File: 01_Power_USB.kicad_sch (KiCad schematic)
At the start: 11 parts, among them J1 UJC-HP-3-SMT-TR, U3 TLV75533PDBVR, U5 TPD2E2U06DCK

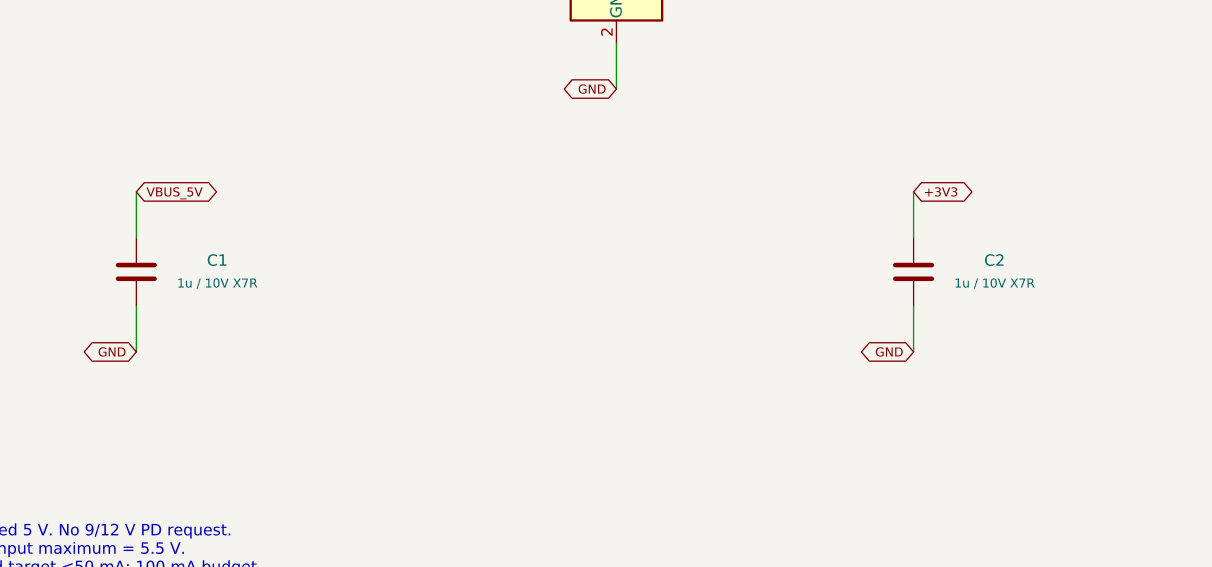
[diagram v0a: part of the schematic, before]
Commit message: Complete procurement BOM and document component review gates
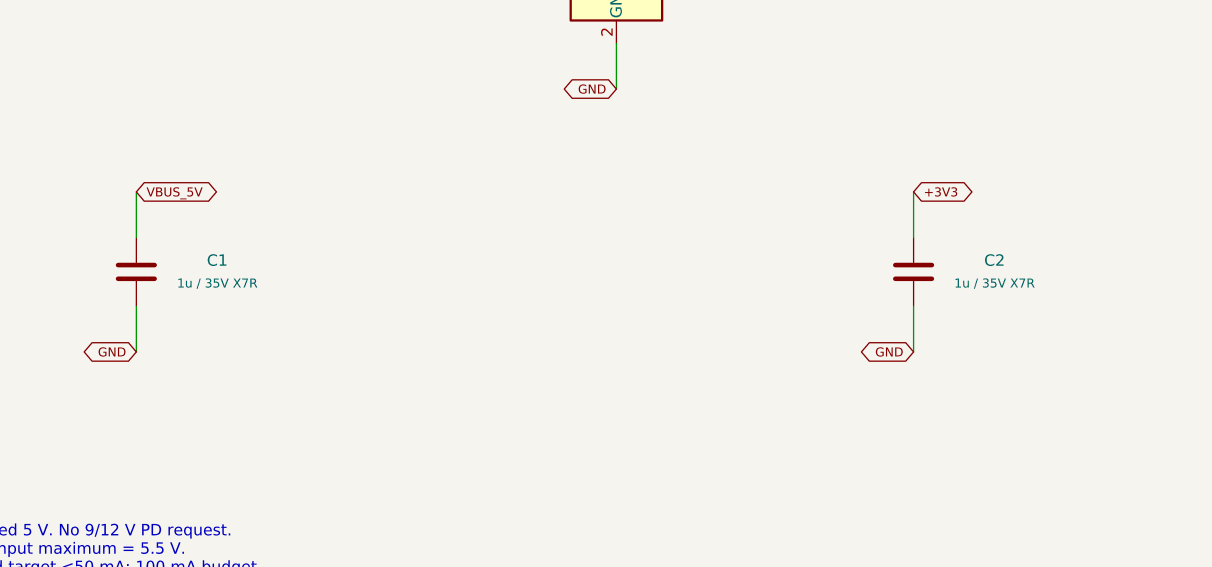
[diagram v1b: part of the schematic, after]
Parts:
- C1, C2: value 1u / 10V X7R -> 1u / 35V X7R; MPN (none) -> C1608X7R1V105K080AC; Manufacturer (none) -> TDK
- D91, U3, U5: Manufacturer (none) -> Texas Instruments
- J1: Manufacturer (none) -> Same Sky
- R1, R2: MPN (none) -> ERJ3EKF5101V; Manufacturer (none) -> Panasonic Industry
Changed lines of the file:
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@@
         (font
           (size 1.27 1.27)) hide))
-    (property "Datasheet" "https://www.usb.org/sites/default/files/documents/usb_type-c.zip"
+    (property "Datasheet" "https://www.sameskydevices.com/product/resource/ujc-hp-3-smt-tr.pdf"
       (at 50.8 71.12 0)
       (effects
@@
           (size 1.27 1.27)) hide))
     (property "MPN" "UJC-HP-3-SMT-TR"
+      (at 50.8 71.12 0)
+      (effects
+        (font
+          (size 1.27 1.27)) hide))
+    (property "Manufacturer" "Same Sky"
       (at 50.8 71.12 0)
       (effects
@@
         (font
           (size 1.27 1.27)) hide))
-    (property "Datasheet" ""
+    (property "Datasheet" "https://industrial.panasonic.com/cdbs/www-data/pdf/RDA0000/AOA0000C304.pdf"
       (at 104.14 81.28 0)
       (effects
         (font
           (size 1.27 1.27)) hide))
-    (property "MPN" ""
+    (property "MPN" "ERJ3EKF5101V"
+      (at 104.14 81.28 0)
+      (effects
+        (font
+          (size 1.27 1.27)) hide))
+    (property "Manufacturer" "Panasonic Industry"
       (at 104.14 81.28 0)
       (effects
@@
         (font
           (size 1.27 1.27)) hide))
-    (property "Datasheet" ""
+    (property "Datasheet" "https://industrial.panasonic.com/cdbs/www-data/pdf/RDA0000/AOA0000C304.pdf"
       (at 139.7 81.28 0)
       (effects
         (font
           (size 1.27 1.27)) hide))
-    (property "MPN" ""
+    (property "MPN" "ERJ3EKF5101V"
+      (at 139.7 81.28 0)
+      (effects
+        (font
+          (size 1.27 1.27)) hide))
+    (property "Manufacturer" "Panasonic Industry"
       (at 139.7 81.28 0)
       (effects
@@
         (font
           (size 1.27 1.27)) hide))
-    (property "Datasheet" "http://www.ti.com/lit/ds/symlink/tpd2e2u06.pdf"
+    (property "Datasheet" "https://www.ti.com/lit/ds/symlink/tpd2e2u06.pdf"
       (at 83.82 182.88 0)
       (effects
@@
           (size 1.27 1.27)) hide))
     (property "MPN" "TPD2E2U06DCKR"
+      (at 83.82 182.88 0)
+      (effects
+        (font
+          (size 1.27 1.27)) hide))
+    (property "Manufacturer" "Texas Instruments"
       (at 83.82 182.88 0)
       (effects
@@
         (font
           (size 1.27 1.27)) hide))
-    (property "Datasheet" ""
+    (property "Datasheet" "https://www.ti.com/lit/ds/symlink/tpd1e10b06.pdf"
       (at 152.4 182.88 0)
       (effects
@@
           (size 1.27 1.27)) hide))
     (property "MPN" "TPD1E10B06DYAR"
+      (at 152.4 182.88 0)
+      (effects
+        (font
+          (size 1.27 1.27)) hide))
+    (property "Manufacturer" "Texas Instruments"
       (at 152.4 182.88 0)
       (effects
@@
         (font
           (size 1.27 1.27)) hide))
-    (property "Datasheet" "http://www.ti.com/lit/ds/symlink/tlv755p.pdf"
+    (property "Datasheet" "https://www.ti.com/lit/ds/symlink/tlv755p.pdf"
       (at 292.1 71.12 0)
       (effects
@@
           (size 1.27 1.27)) hide))
     (property "MPN" "TLV75533PDBVR"
+      (at 292.1 71.12 0)
+      (effects
+        (font
+          (size 1.27 1.27)) hide))
+    (property "Manufacturer" "Texas Instruments"
       (at 292.1 71.12 0)
       (effects
@@
         (font
           (size 1.27 1.27))))
-    (property "Value" "1u / 10V X7R"
+    (property "Value" "1u / 35V X7R"
       (at 247.76 105.41 0)
       (effects
@@
         (font
           (size 1.27 1.27)) hide))
-    (property "Datasheet" ""
+    (property "Datasheet" "https://product.tdk.com/system/files/dam/doc/product/capacitor/ceramic/mlcc/charasheet/c1608x7r1v105k080ac.pdf"
       (at 238.76 104.14 0)
       (effects
         (font
           (size 1.27 1.27)) hide))
-    (property "MPN" ""
+    (property "MPN" "C1608X7R1V105K080AC"
+      (at 238.76 104.14 0)
+      (effects
+        (font
+          (size 1.27 1.27)) hide))
+    (property "Manufacturer" "TDK"
       (at 238.76 104.14 0)
       (effects
@@
         (font
           (size 1.27 1.27))))
-    (property "Value" "1u / 10V X7R"
+    (property "Value" "1u / 35V X7R"
       (at 334.12 105.41 0)
       (effects
@@
         (font
           (size 1.27 1.27)) hide))
-    (property "Datasheet" ""
+    (property "Datasheet" "https://product.tdk.com/system/files/dam/doc/product/capacitor/ceramic/mlcc/charasheet/c1608x7r1v105k080ac.pdf"
       (at 325.12 104.14 0)
       (effects
         (font
           (size 1.27 1.27)) hide))
-    (property "MPN" ""
+    (property "MPN" "C1608X7R1V105K080AC"
+      (at 325.12 104.14 0)
+      (effects
+        (font
+          (size 1.27 1.27)) hide))
+    (property "Manufacturer" "TDK"
       (at 325.12 104.14 0)
       (effects
@@
         (font
           (size 1.27 1.27)) hide))
+    (property "Manufacturer" ""
+      (at 231.14 210.82 0)
+      (effects
+        (font
+          (size 1.27 1.27)) hide))
     (pin "1"
 )
@@
         (font
           (size 1.27 1.27)) hide))
+    (property "Manufacturer" ""
+      (at 292.1 210.82 0)
+      (effects
+        (font
+          (size 1.27 1.27)) hide))
     (pin "1"
 )
@@
       (at 353.06 210.82 0)
       (effects
+        (font
+          (size 1.27 1.27)) hide))
+    (property "Manufacturer" ""
+      (at 353.06 210.82 0)
+      (effects
